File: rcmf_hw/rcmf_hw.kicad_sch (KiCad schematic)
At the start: 18 parts, among them M1 Motor_DC, M2 Motor_DC, U1 LM2596-5V, U2 DRV8833, U3 ESP32-WROOM-32, U4 AMS1117-3.3

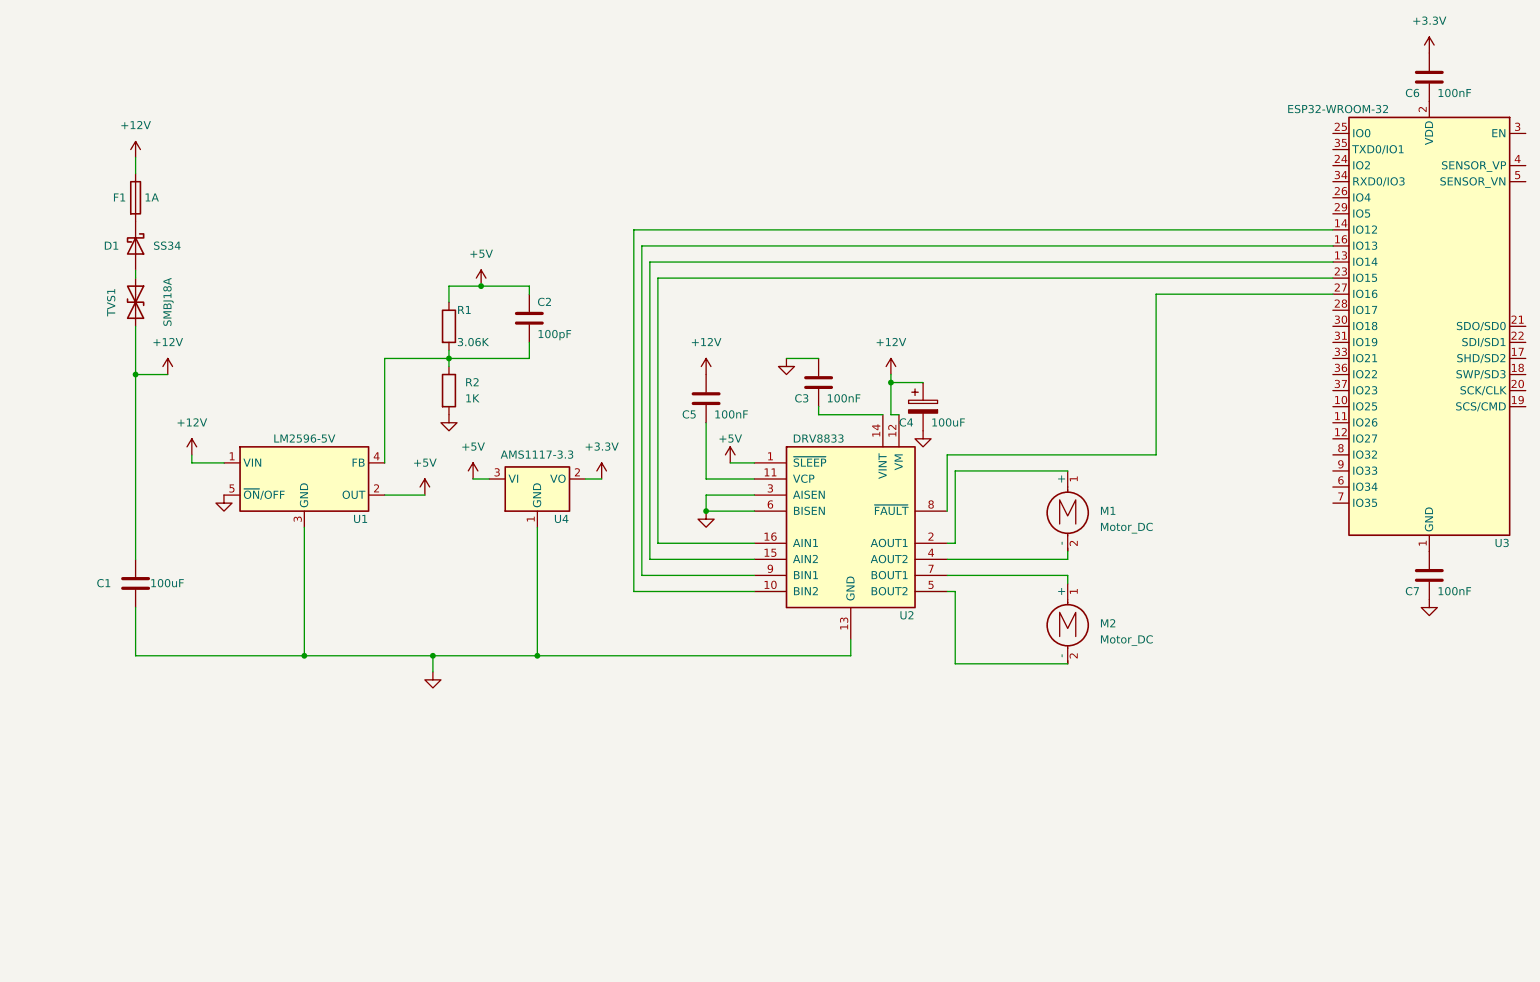
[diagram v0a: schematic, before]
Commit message: Revisione dello schema, aggiunto Buck per generare la 3,3 pertendo dalla 6
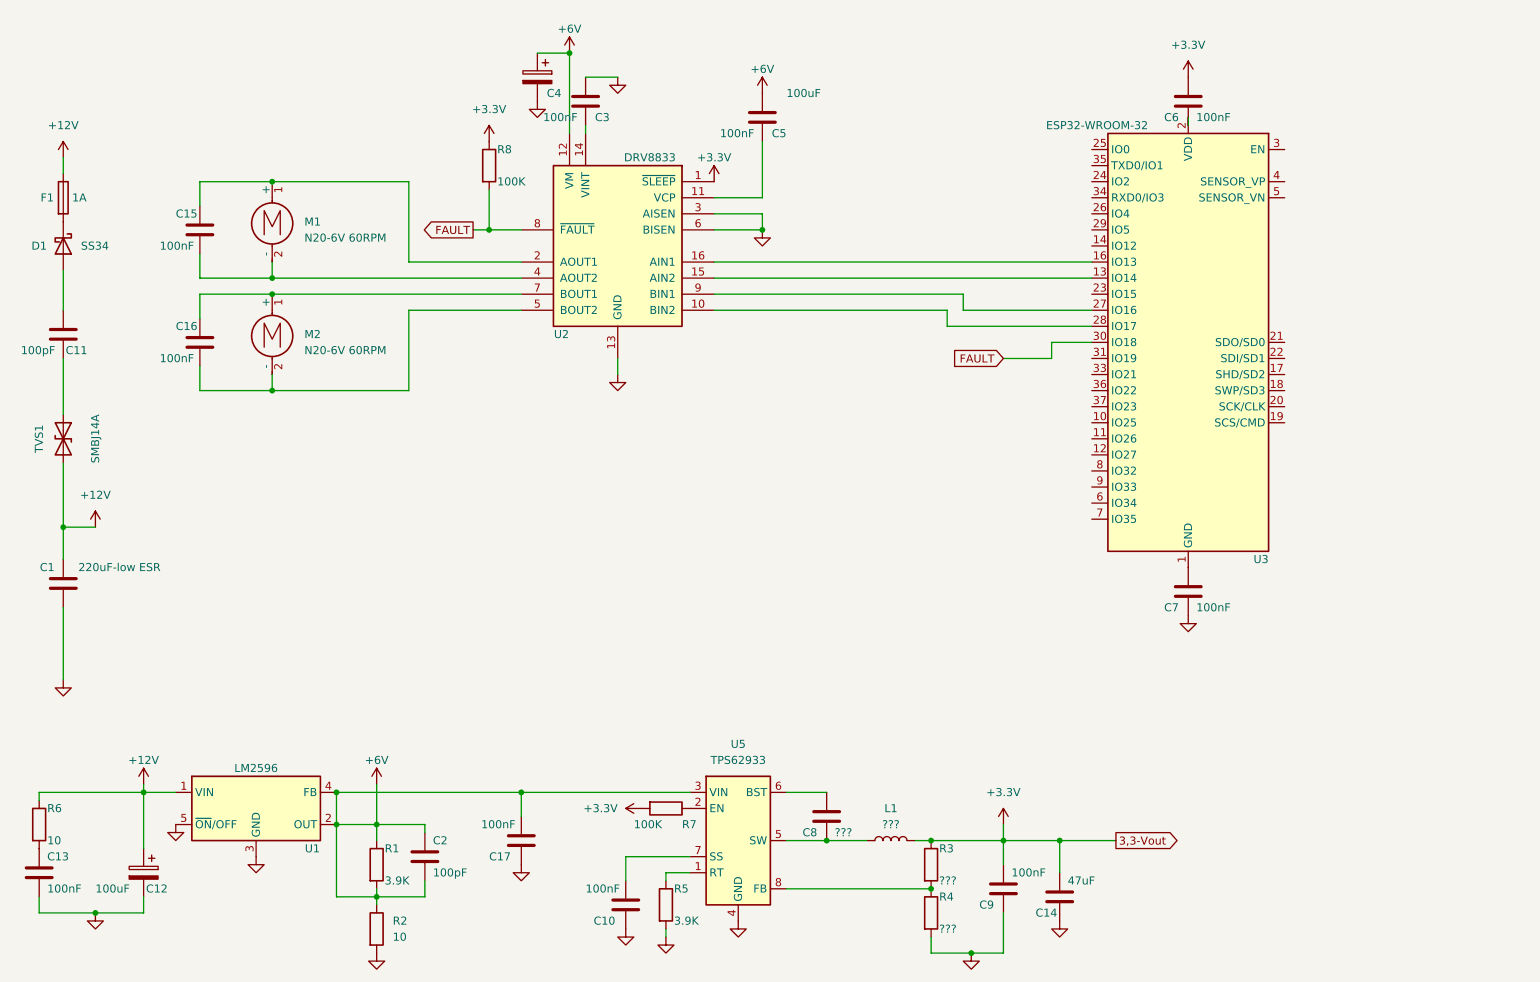
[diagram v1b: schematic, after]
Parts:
- removed U4: AMS1117-3.3, Package_TO_SOT_SMD:SOT-223-3_TabPin2, symbol Regulator_Linear:AMS1117-3.3
- added C10, C13, C15, C16, C17, C9: 100nF, symbol Device:C
- added C11: 100pF, symbol Device:C
- added C12: 100uF, symbol Device:C_Polarized
- added C14: 47uF, symbol Device:C
- added C8: ???, symbol Device:C
- added L1: ???, symbol Device:L
- added R3, R4: ???, symbol Device:R
- added R5: 3.9K, symbol Device:R
- added R6: 10, symbol Device:R
- added R7, R8: 100K, symbol Device:R
- added U5: TPS62933, Package_TO_SOT_SMD:SOT-583-8, symbol Regulator_Switching:TPS62933
- C1: value 100uF -> 220uF-low ESR
- M1, M2: value Motor_DC -> N20-6V 60RPM
- R1: value 3.06K -> 3.9K
- R2: value 1K -> 10
- TVS1: value SMBJ18A -> SMBJ14A
- U1: value LM2596-5V -> LM2596
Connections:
- net +12V: now also C12.1, R6.1; no longer C4.1, C5.1, U2.12 (VM)
- net +3.3V: now also U2.1 (~{SLEEP}), C14.1, C9.1, L1.2, R3.1, R7.2, R8.1
- net GND: now also C10.2, C12.2, C13.2, C14.2, C17.2, C9.2, R4.2, R5.2, U5.4 (GND)
- net +6V: now reaches C2.2, R1.2, R2.1, U1.4 (FB)
- net +6V: now also C2.1, C4.1, C5.1, R1.1, U1.2 (OUT), U2.12 (VM), C17.1, U5.3 (VIN)
- net at TVS1.1 (A1): now also C11.2; no longer D1.2 (A)
- net at M2.1 (+), U2.7 (BOUT1): now also C16.2
- net at M2.2 (-), U2.5 (BOUT2): now also C16.1
- net at U3.14 (IO12): no longer U2.10 (BIN2)
- net at U3.16 (IO13): now also U2.16 (AIN1); no longer U2.9 (BIN1)
- net at U3.23 (IO15): no longer U2.16 (AIN1)
- net at U3.27 (IO16): now also U2.9 (BIN1); no longer U2.8 (~{FAULT})
- net at U3.28 (IO17): now also U2.10 (BIN2)
- net FAULT: now reaches U3.30 (IO18)
- net FAULT: now also U2.8 (~{FAULT}), R8.2
- net at M1.1 (+), U2.2 (AOUT1): now also C15.2
- net at M1.2 (-), U2.4 (AOUT2): now also C15.1
- removed net +5V: C2.1, R1.1, U1.2 (OUT), U2.1 (~{SLEEP})
- new net: C8.2, L1.1, U5.5 (SW)
- new net: C11.1, D1.2 (A)
- new net: R3.2, R4.1, U5.8 (FB)
- new net: R5.1, U5.1 (RT)
- new net: C8.1, U5.6 (BST)
- new net: C10.1, U5.7 (SS)
- new net: C13.1, R6.2
- new net: R7.1, U5.2 (EN)
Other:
- moved on the sheet: C1, C2, C3, C4, C5, C6, C7, D1, F1, M1, M2, R1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
